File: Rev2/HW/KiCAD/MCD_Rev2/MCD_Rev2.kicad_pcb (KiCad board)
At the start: 2 copper layers, 196.3 x 114.7 mm, 76 parts, among them J1 DBUS_LOW, J2 DBUS_HIGH, J3 ABUS, J4 POWER, J5 JTAG, J6 Conn_01x02_Male, J7 DUART A, J8 DUART B, SW1 SW_Push, U1 XC9572XL-PC44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

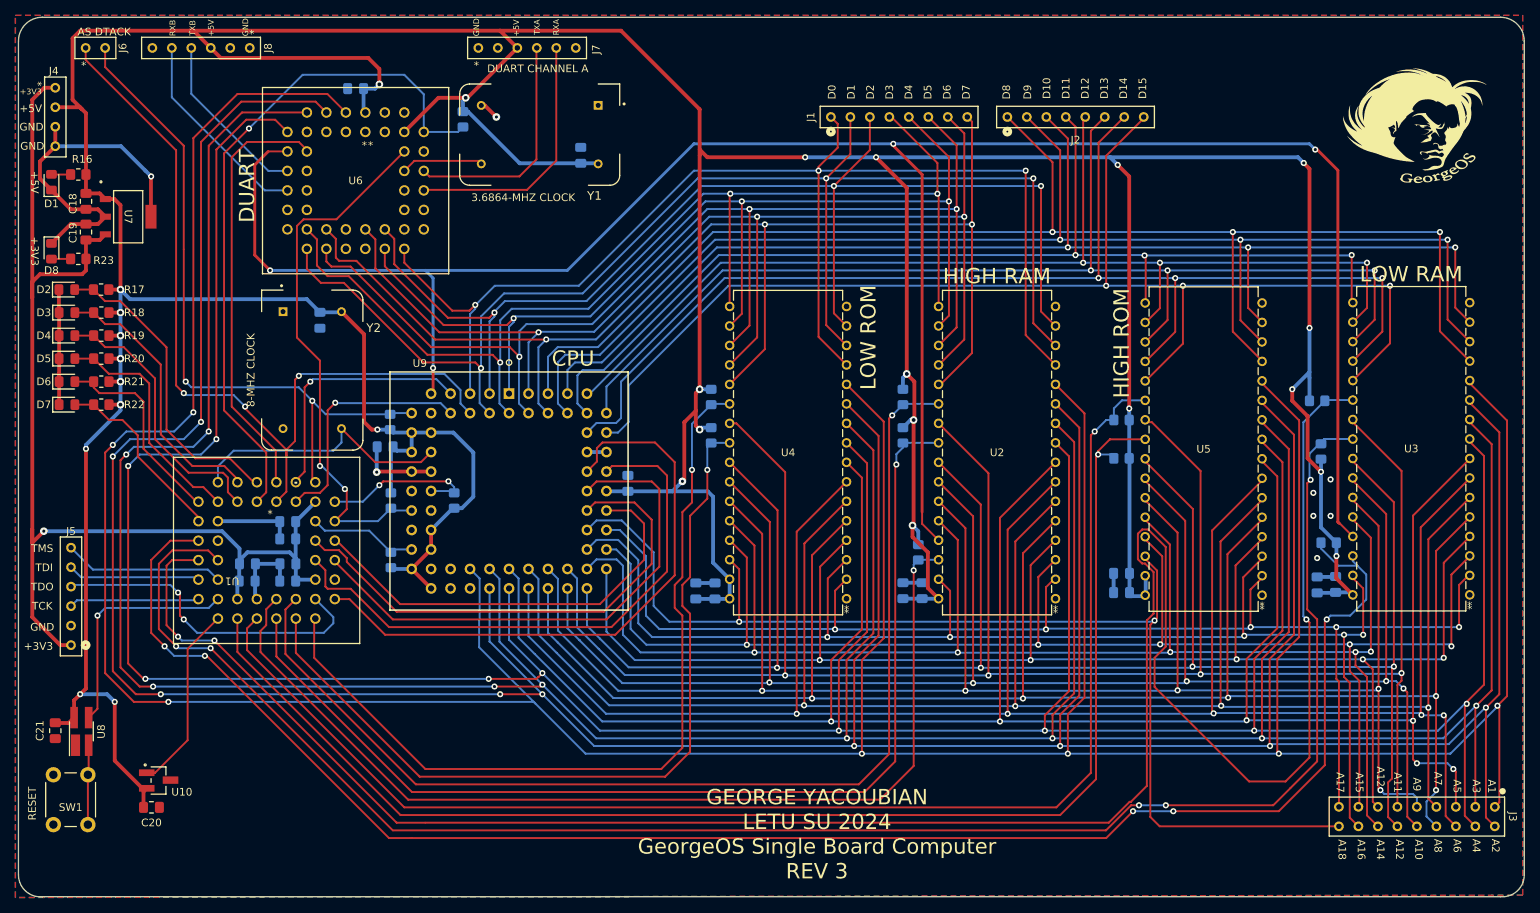
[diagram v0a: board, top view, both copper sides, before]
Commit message: spaced out traces EVEN MORE
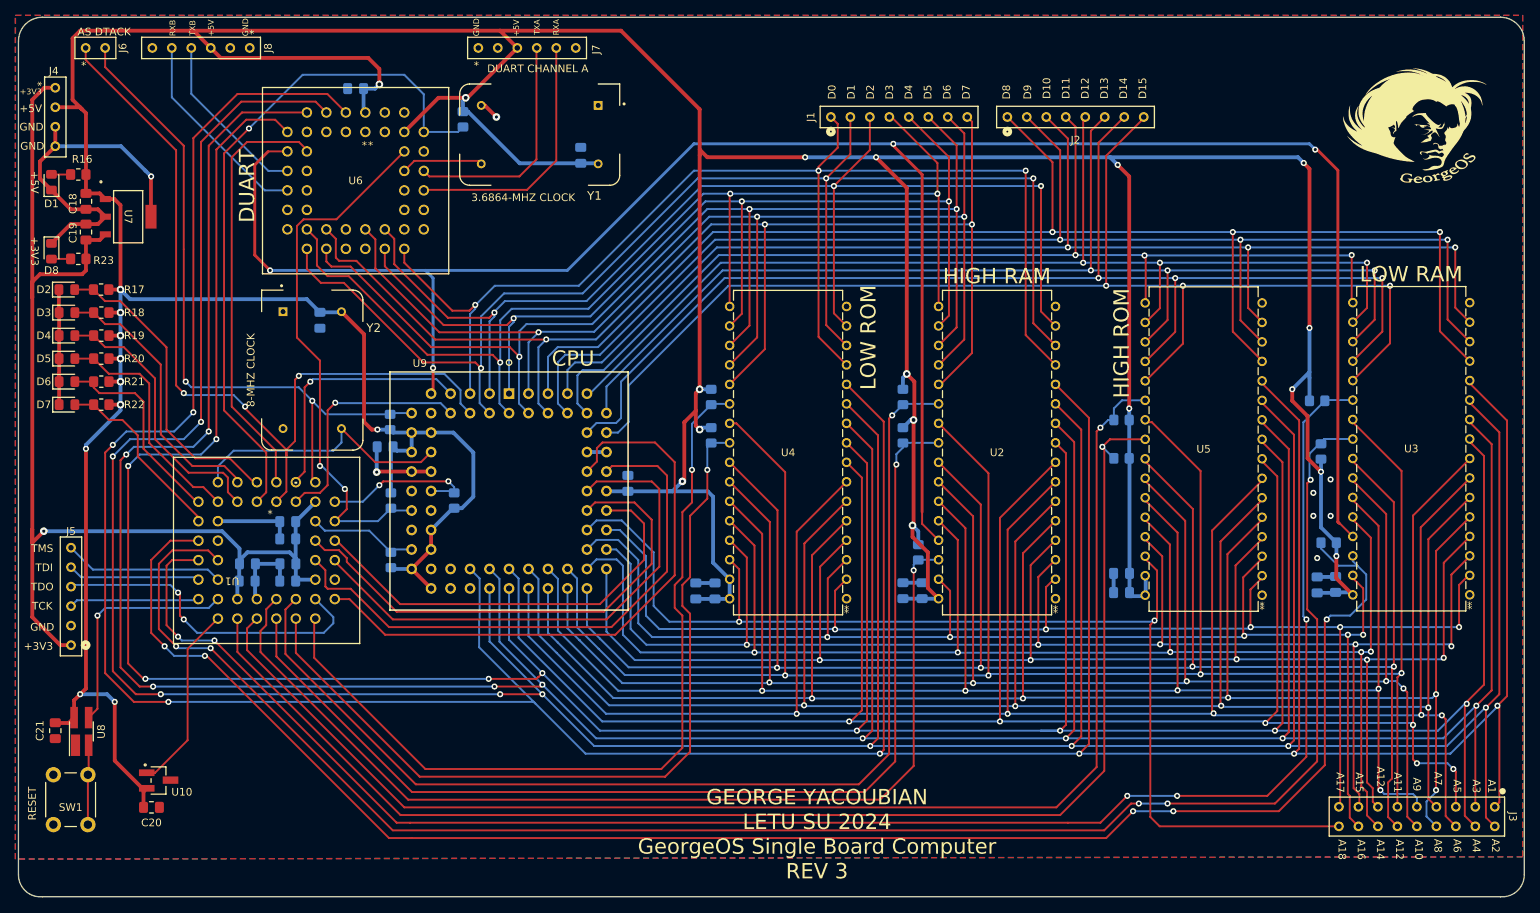
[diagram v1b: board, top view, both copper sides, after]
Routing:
- net RAMHCE: track 288.9 -> 226.5 mm, vias 3 -> 5
- net A3: track 476.1 -> 473.4 mm
- net A2: track 499.4 -> 497.0 mm
- net A1: track 523.3 -> 521.2 mm
- net A5: track 292.9 -> 291.5 mm
- net A4: track 454.3 -> 453.0 mm

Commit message: filled in POURS
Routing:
- net A18: track 152.5 -> 148.5 mm, vias 2 -> 4
- net RAMHCE2: track 222.9 -> 224.2 mm
- net A1: track 521.2 -> 522.4 mm, vias 7 -> 6
- net RAMHOE: track 230.4 -> 230.9 mm
- net RAMHCE: track 226.5 -> 226.2 mm, vias 5 -> 3

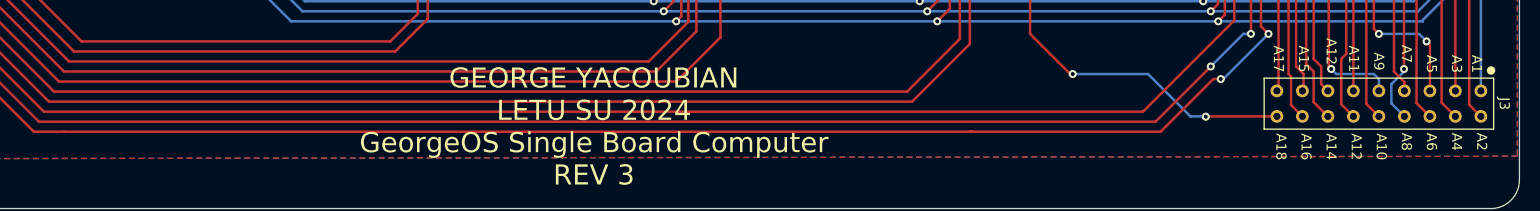
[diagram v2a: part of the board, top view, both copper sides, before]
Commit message: added via stitching, now adjusting silkscreen
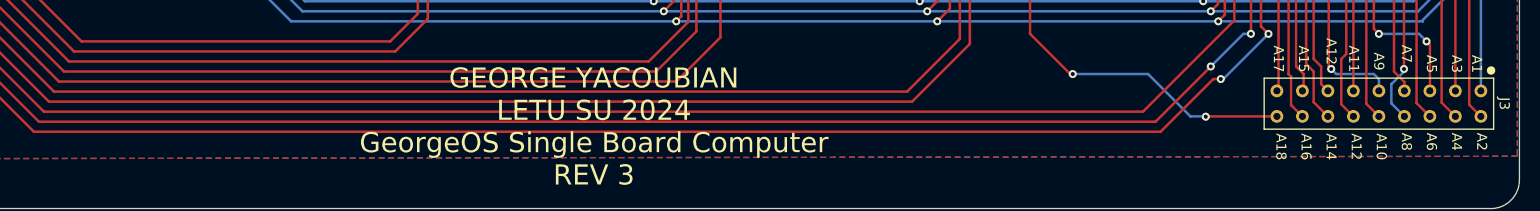
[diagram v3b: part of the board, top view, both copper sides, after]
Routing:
- net A1: track 522.4 -> 521.9 mm
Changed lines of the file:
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@@
   (segment (start 178.86 125.64) (end 180.25 124.25) (width 0.254) (layer "B.Cu") (net 26))
   (segment (start 180.25 119.5) (end 193.25 106.5) (width 0.254) (layer "B.Cu") (net 26))
-  (segment (start 293.16 174.431105) (end 293.52056 174.070545) (width 0.25) (layer "F.Cu") (net 27))
   (segment (start 240.25 166.25) (end 240.25 123.72) (width 0.254) (layer "F.Cu") (net 27))
   (segment (start 112 157) (end 115.75 160.75) (width 0.254) (layer "F.Cu") (net 27))
@@
   (segment (start 119.75 153.5) (end 118 151.75) (width 0.25) (layer "F.Cu") (net 69))
   (segment (start 149 178.5) (end 151.75 178.5) (width 0.25) (layer "F.Cu") (net 69))
+  (segment (start 261.25 178.5) (end 266.5 173.25) (width 0.254) (layer "F.Cu") (net 69))
   (segment (start 271.25 168) (end 271.25 150) (width 0.254) (layer "F.Cu") (net 69))
   (segment (start 120.52 139.73) (end 124.16 139.73) (width 0.25) (layer "F.Cu") (net 69))
-  (segment (start 261.25 178.5) (end 242.25 178.5) (width 0.254) (layer "F.Cu") (net 69))
-  (segment (start 266.5 173.25) (end 261.25 178.5) (width 0.254) (layer "F.Cu") (net 69))
+  (segment (start 151.75 178.5) (end 261.25 178.5) (width 0.254) (layer "F.Cu") (net 69))
   (segment (start 118 151.75) (end 118 142.25) (width 0.25) (layer "F.Cu") (net 69))
-  (segment (start 152 178.5) (end 151.75 178.5) (width 0.254) (layer "F.Cu") (net 69))
-  (segment (start 242.5 178.5) (end 242.25 178.5) (width 0.254) (layer "F.Cu") (net 69))
   (segment (start 125 154.75) (end 125.25 154.75) (width 0.25) (layer "F.Cu") (net 69))
   (segment (start 272 168.75) (end 271.25 168) (width 0.254) (layer "F.Cu") (net 69))
-  (segment (start 267.25 173.25) (end 266.5 173.25) (width 0.254) (layer "F.Cu") (net 69))
-  (segment (start 242.25 178.5) (end 152 178.5) (width 0.254) (layer "F.Cu") (net 69))
+  (segment (start 266.5 173.25) (end 267.25 173.25) (width 0.254) (layer "F.Cu") (net 69))
   (segment (start 118 142.25) (end 120.52 139.73) (width 0.25) (layer "F.Cu") (net 69))
   (segment (start 125.25 154.75) (end 149 178.5) (width 0.25) (layer "F.Cu") (net 69))
